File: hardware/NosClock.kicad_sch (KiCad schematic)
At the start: 32 parts, among them J101 USB_C_Receptacle_USB2.0_16P, J102 Conn_01x02, J103 Conn_01x04, J104 12V IN, U101 ESP32-C3-MINI-1, U103 DS3231MZ

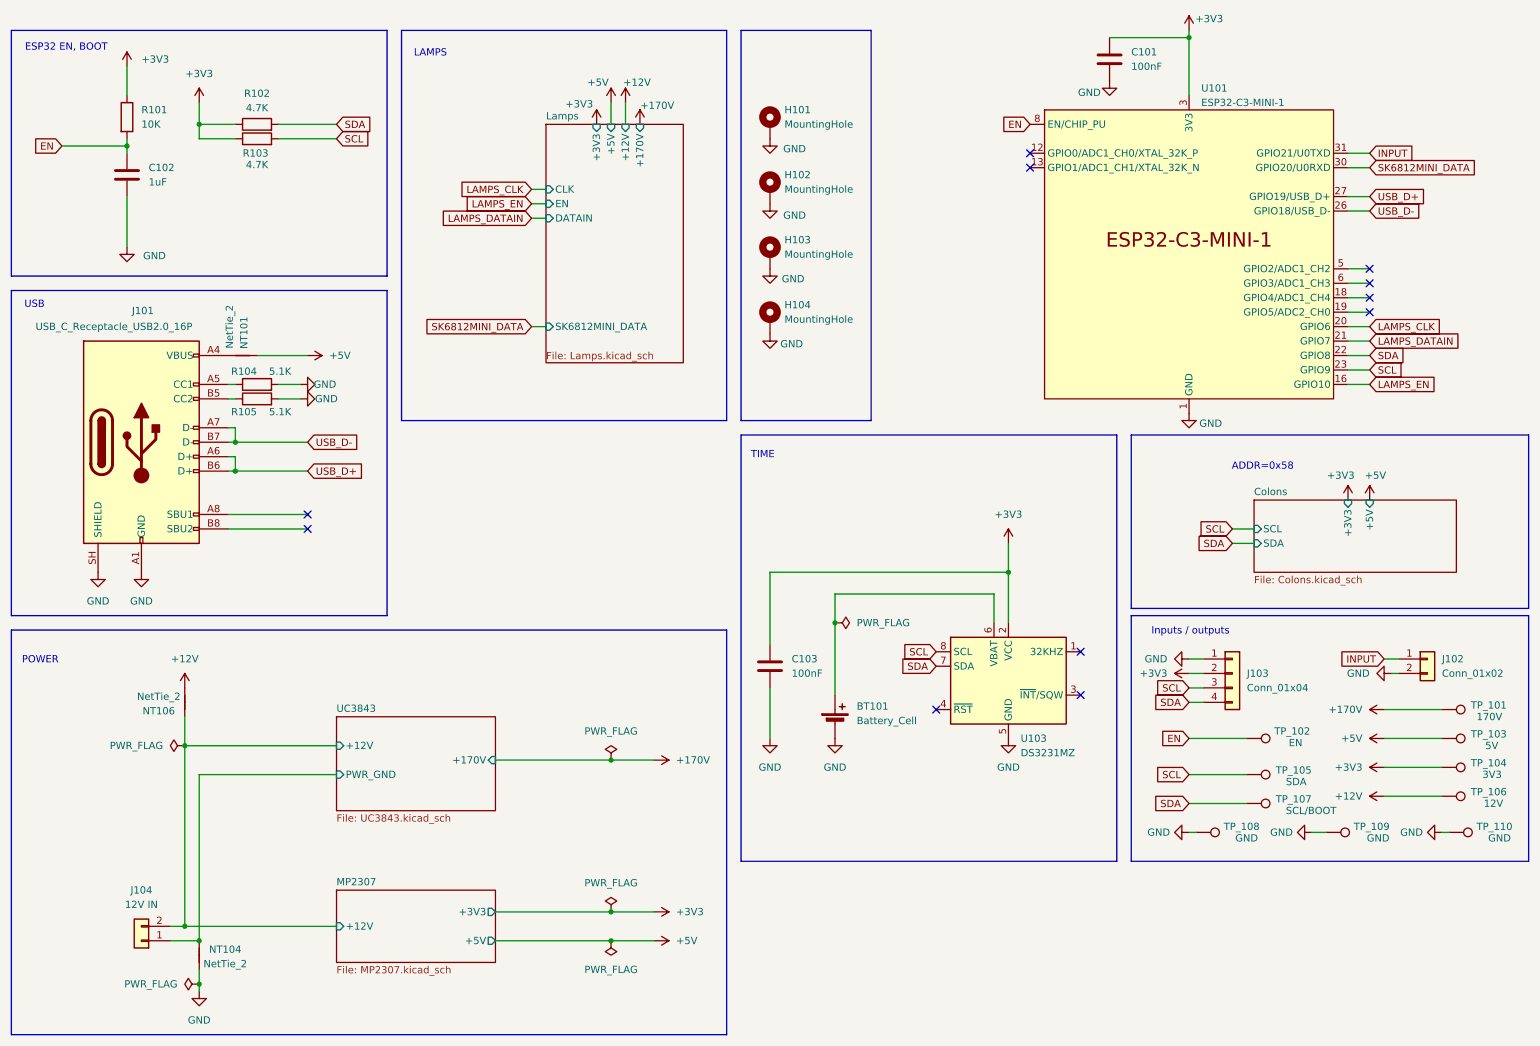
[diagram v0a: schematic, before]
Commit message: Fix lamps footprints
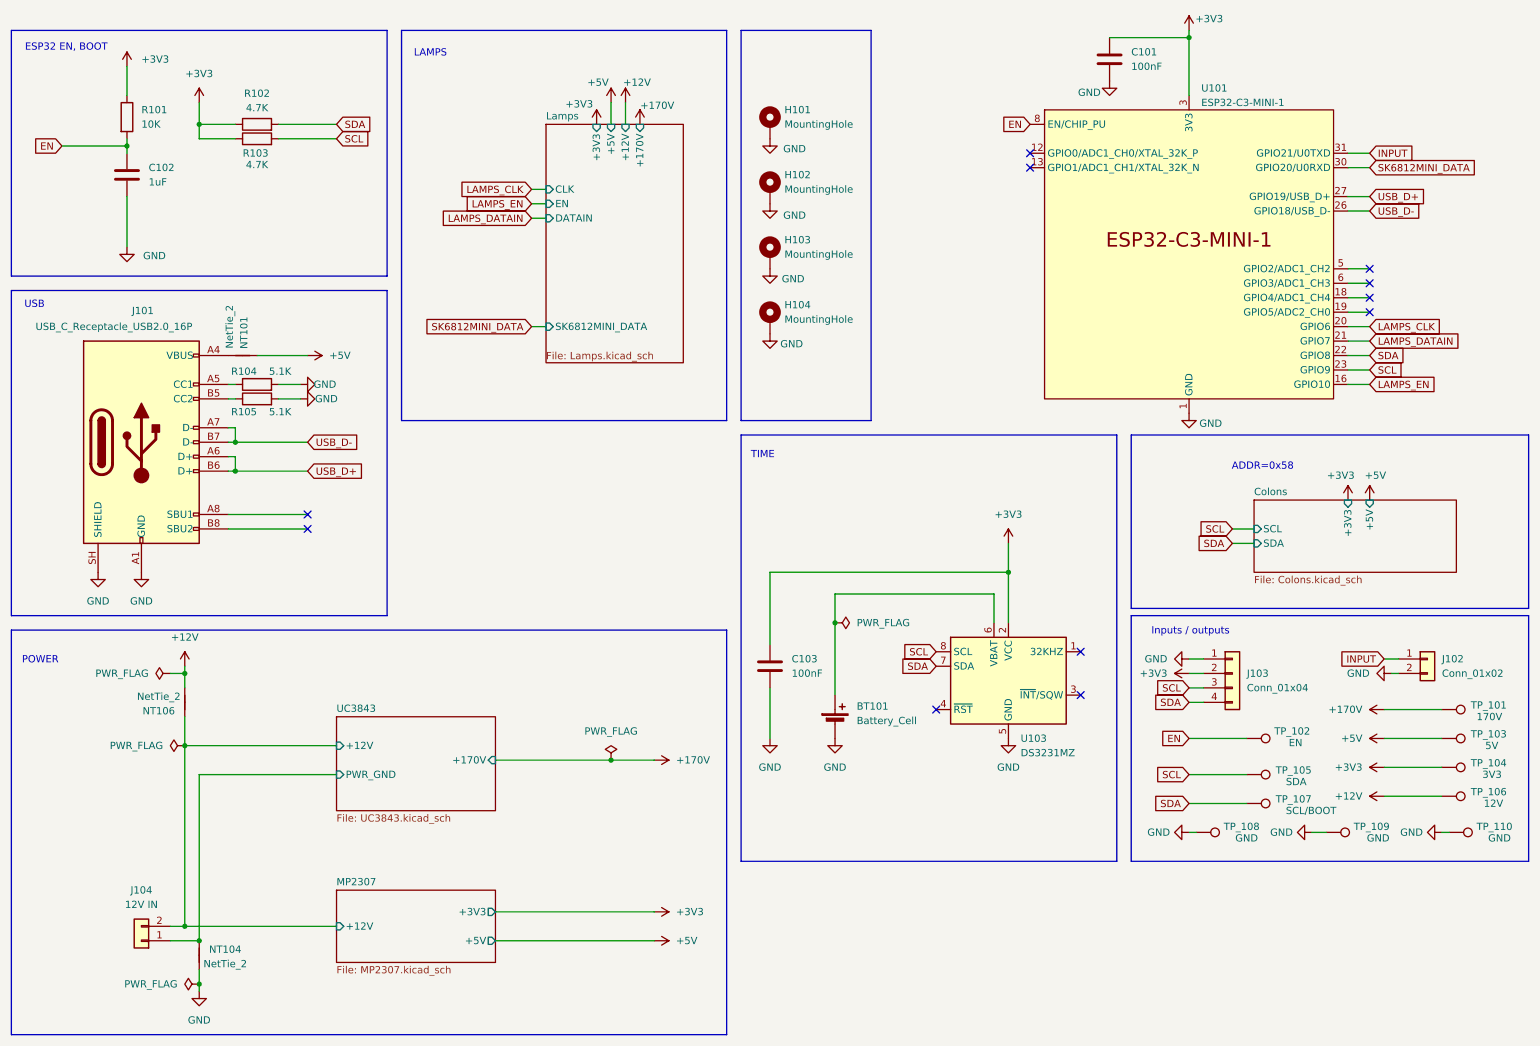
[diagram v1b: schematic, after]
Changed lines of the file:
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@@
 	)
 	(junction
-		(at 121.92 176.53)
-		(diameter 0)
-		(color 0 0 0 0)
-	)
-	(junction
 		(at 161.29 120.65)
 		(diameter 0)
@@
 	)
 	(junction
-		(at 121.92 171.45)
+		(at 36.83 36.83)
 		(diameter 0)
 		(color 0 0 0 0)
 	)
 	(junction
-		(at 36.83 36.83)
+		(at 121.92 144.78)
 		(diameter 0)
 		(color 0 0 0 0)
 	)
 	(junction
-		(at 121.92 144.78)
+		(at 223.52 17.78)
 		(diameter 0)
 		(color 0 0 0 0)
 	)
 	(junction
-		(at 223.52 17.78)
+		(at 46.99 129.54)
 		(diameter 0)
 		(color 0 0 0 0)
@@
 	)
 	(no_connect
-		(at 179.07 135.89)
+		(at 255.27 58.42)
 	)
 	(no_connect
-		(at 255.2472 58.42)
+		(at 179.07 135.89)
 	)
 	(wire
@@
 	(wire
 		(pts
-			(xy 129.54 171.45) (xy 121.92 171.45)
+			(xy 36.83 22.86) (xy 36.83 27.94)
 		)
 		(stroke
@@
 	(wire
 		(pts
-			(xy 36.83 22.86) (xy 36.83 27.94)
+			(xy 46.99 129.54) (xy 46.99 132.08)
 		)
 		(stroke
@@
 	(wire
 		(pts
-			(xy 101.6 176.53) (xy 121.92 176.53)
-		)
-		(stroke
-			(width 0)
-			(type default)
-		)
-	)
-	(wire
-		(pts
 			(xy 46.99 142.24) (xy 73.66 142.24)
 		)
@@
 	(wire
 		(pts
-			(xy 129.54 176.53) (xy 121.92 176.53)
+			(xy 101.6 176.53) (xy 129.54 176.53)
 		)
 		(stroke
@@
 	(wire
 		(pts
+			(xy 251.46 58.42) (xy 255.27 58.42)
+		)
+		(stroke
+			(width 0)
+			(type default)
+		)
+	)
+	(wire
+		(pts
 			(xy 46.99 173.99) (xy 73.66 173.99)
 		)
@@
 	(wire
 		(pts
-			(xy 255.27 58.42) (xy 251.46 58.42)
+			(xy 46.99 128.27) (xy 46.99 129.54)
 		)
 		(stroke
@@
 	(wire
 		(pts
-			(xy 101.6 171.45) (xy 121.92 171.45)
+			(xy 101.6 171.45) (xy 129.54 171.45)
 		)
 		(stroke
@@
 	(wire
 		(pts
+			(xy 44.45 129.54) (xy 46.99 129.54)
+		)
+		(stroke
+			(width 0)
+			(type default)
+		)
+	)
+	(wire
+		(pts
 			(xy 68.58 101.6) (xy 54.61 101.6)
 		)
@@
 	)
 	(symbol
+		(lib_id "power:PWR_FLAG")
+		(at 44.45 129.54 90)
+		(unit 1)
+		(body_style 1)
+		(exclude_from_sim no)
+		(in_bom yes)
+		(on_board yes)
+		(in_pos_files yes)
+		(dnp no)
+		(fields_autoplaced yes)
+		(property "Reference" "#FLG0104"
+			(at 42.545 129.54 0)
+			(hide yes)
+			(show_name no)
+			(do_not_autoplace no)
+			(effects
+				(font
+					(size 1.27 1.27)
+				)
+			)
+		)
+		(property "Value" "PWR_FLAG"
+			(at 40.64 129.5399 90)
+			(show_name no)
+			(do_not_autoplace no)
+			(effects
+				(font
+					(size 1.27 1.27)
+				)
+				(justify left)
+			)
+		)
+		(property "Footprint" ""
+			(at 44.45 129.54 0)
+			(hide yes)
+			(show_name no)
+			(do_not_autoplace no)
+			(effects
+				(font
+					(size 1.27 1.27)
+				)
+			)
+		)
+		(property "Datasheet" ""
+			(at 44.45 129.54 0)
+			(hide yes)
+			(show_name no)
+			(do_not_autoplace no)
+			(effects
+				(font
+					(size 1.27 1.27)
+				)
+			)
+		)
+		(property "Description" "Special symbol for telling ERC where power comes from"
+			(at 44.45 129.54 0)
+			(hide yes)
+			(show_name no)
+			(do_not_autoplace no)
+			(effects
+				(font
+					(size 1.27 1.27)
+				)
+			)
+		)
+		(pin "1"
+		)
+		(instances
+			(project "NosClock"
+				(path "/5a46aee9-b968-477e-a4a1-4edba06163a3"
+					(reference "#FLG0104")
+					(unit 1)
+				)
+			)
+		)
+	)
+	(symbol
 		(lib_id "power:GND")
 		(at 267.97 157.48 270)
@@
 			)
 		)
+		(property "Sim.Device" "V"
+			(at 161.29 138.43 0)
+			(hide yes)
+			(show_name no)
+			(do_not_autoplace no)
+			(effects
+				(font
+					(size 1.27 1.27)
+				)
+			)
+		)
+		(property "Sim.Type" "DC"
+			(at 161.29 138.43 0)
+			(hide yes)
+			(show_name no)
+			(do_not_autoplace no)
+			(effects
+				(font
+					(size 1.27 1.27)
+				)
+			)
+		)
+		(property "Sim.Pins" "1=+ 2=-"
+			(at 161.29 138.43 0)
+			(hide yes)
+			(show_name no)
+			(do_not_autoplace no)
+			(effects
+				(font
+					(size 1.27 1.27)
+				)
+			)
+		)
 		(pin "1"
 		)
@@
 	)
 	(symbol
-		(lib_id "power:PWR_FLAG")
-		(at 121.92 171.45 0)
-		(unit 1)
-		(body_style 1)
-		(exclude_from_sim no)
-		(in_bom yes)
-		(on_board yes)
-		(in_pos_files yes)
-		(dnp no)
-		(fields_autoplaced yes)
-		(property "Reference" "#FLG0104"
-			(at 121.92 169.545 0)
-			(hide yes)
-			(show_name no)
-			(do_not_autoplace no)
-			(effects
-				(font
-					(size 1.27 1.27)
-				)
-			)
-		)
-		(property "Value" "PWR_FLAG"
-			(at 121.92 166.37 0)
-			(show_name no)
-			(do_not_autoplace no)
-			(effects
-				(font
-					(size 1.27 1.27)
-				)
-			)
-		)
-		(property "Footprint" ""
-			(at 121.92 171.45 0)
-			(hide yes)
-			(show_name no)
-			(do_not_autoplace no)
-			(effects
-				(font
-					(size 1.27 1.27)
-				)
-			)
-		)
-		(property "Datasheet" ""
-			(at 121.92 171.45 0)
-			(hide yes)
-			(show_name no)
-			(do_not_autoplace no)
-			(effects
-				(font
-					(size 1.27 1.27)
-				)
-			)
-		)
-		(property "Description" "Special symbol for telling ERC where power comes from"
-			(at 121.92 171.45 0)
-			(hide yes)
-			(show_name no)
-			(do_not_autoplace no)
-			(effects
-				(font
-					(size 1.27 1.27)
-				)
-			)
-		)
-		(pin "1"
-		)
-		(instances
-			(project "NosClock"
-				(path "/5a46aee9-b968-477e-a4a1-4edba06163a3"
-					(reference "#FLG0104")
-					(unit 1)
-				)
-			)
-		)
-	)
-	(symbol
 		(lib_id "power:GND")
 		(at 149.86 35.56 0)
@@
 	(symbol
 		(lib_id "power:+3.3V")
-		(at 46.99 132.08 0)
+		(at 46.99 128.27 0)
 		(unit 1)
 		(body_style 1)
@@
 		(fields_autoplaced yes)
 		(property "Reference" "#PWR0130"
-			(at 46.99 135.89 0)
+			(at 46.99 132.08 0)
 			(hide yes)
 			(show_name no)
@@
 		)
 		(property "Value" "+12V"
-			(at 46.99 127 0)
+			(at 46.99 123.19 0)
 			(show_name no)
 			(do_not_autoplace no)
@@
 		)
 		(property "Footprint" ""
-			(at 46.99 132.08 0)
+			(at 46.99 128.27 0)
 			(hide yes)
 			(show_name no)
@@
 		)
 		(property "Datasheet" ""
-			(at 46.99 132.08 0)
+			(at 46.99 128.27 0)
 			(hide yes)
 			(show_name no)
@@
 		)
 		(property "Description" "Power symbol creates a global label with name \"+3.3V\""
-			(at 46.99 132.08 0)
+			(at 46.99 128.27 0)
 			(hide yes)
 			(show_name no)
@@
 					(unit 1)
 				)
-			)
-		)
-	)
-	(symbol
-		(lib_id "power:PWR_FLAG")
-		(at 121.92 176.53 180)
-		(unit 1)
-		(body_style 1)
-		(exclude_from_sim no)
-		(in_bom yes)
-		(on_board yes)
-		(in_pos_files yes)
-		(dnp no)
-		(fields_autoplaced yes)
-		(property "Reference" "#FLG0105"
-			(at 121.92 178.435 0)
-			(hide yes)
-			(show_name no)
-			(do_not_autoplace no)
-			(effects
-				(font
-					(size 1.27 1.27)
-				)
-			)
-		)
-		(property "Value" "PWR_FLAG"
-			(at 121.92 181.61 0)
-			(show_name no)
-			(do_not_autoplace no)
-			(effects
-				(font
-					(size 1.27 1.27)
-				)
-			)
-		)
-		(property "Footprint" ""
-			(at 121.92 176.53 0)
-			(hide yes)
-			(show_name no)
-			(do_not_autoplace no)
-			(effects
-				(font
-					(size 1.27 1.27)
-				)
-			)
-		)
-		(property "Datasheet" ""
-			(at 121.92 176.53 0)
-			(hide yes)
-			(show_name no)
-			(do_not_autoplace no)
-			(effects
-				(font
-					(size 1.27 1.27)
-				)
-			)
-		)
-		(property "Description" "Special symbol for telling ERC where power comes from"
-			(at 121.92 176.53 0)
-			(hide yes)
-			(show_name no)
-			(do_not_autoplace no)
-			(effects
-				(font
-					(size 1.27 1.27)
-				)
-			)
-		)
-		(pin "1"
-		)
-		(instances
-			(project "NosClock"
-				(path "/5a46aee9-b968-477e-a4a1-4edba06163a3"
-					(reference "#FLG0105")
-					(unit 1)
-				)
